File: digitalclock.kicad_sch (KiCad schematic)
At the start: 7 parts

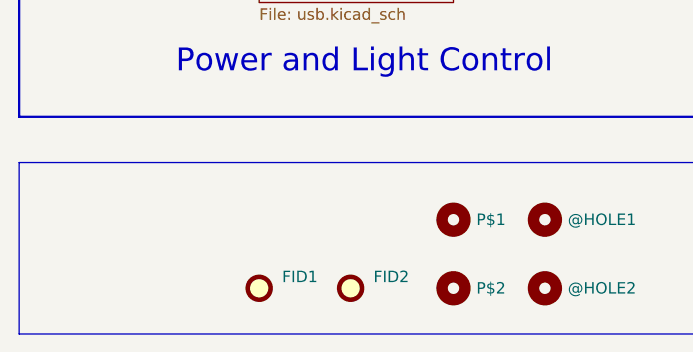
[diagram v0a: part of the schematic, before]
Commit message: Updated BOM, created fab outputs
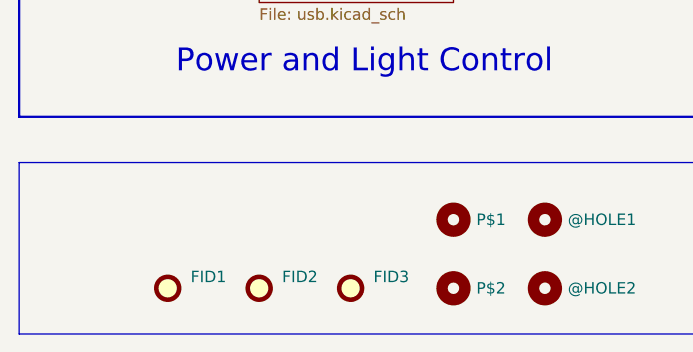
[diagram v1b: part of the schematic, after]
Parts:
- added FID3: Fiducial, Fiducial:Fiducial_1mm_Mask2mm, symbol symbolLibrary:Fiducial
- PCB1: Supplier_1 P/N (none) -> -- mixed values --; Supplier_1 Price @ Qty (none) -> -- mixed values --; Supplier_1 Unit Price (none) -> -- mixed values --
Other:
- moved on the sheet: FID1, FID2
